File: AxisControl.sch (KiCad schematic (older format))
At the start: 2 parts, among them J14 Max, J15 Min

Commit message: Update annotations.
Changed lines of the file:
@@
 EESchema Schematic File Version 4
 LIBS:PrntrBoardV1-cache
-EELAYER 26 0
+EELAYER 29 0
 EELAYER END
 $Descr A4 11693 8268
@@
 AR Path="/5AC337B6/5ACCA309/5AE0BB35" Ref="J16"  Part="1"
 AR Path="/5AC337B6/5ACE1C6D/5AE0BB35" Ref="J18"  Part="1"
-F 0 "J16" H 6500 3567 50  0000 C CNN
+F 0 "J18" H 6500 3567 50  0000 C CNN
 F 1 "Max" H 6500 3476 50  0000 C CNN
 F 2 "Connector_PinHeader_2.54mm:PinHeader_1x02_P2.54mm_Vertical" H 6450 3350 50  0001 C CNN
@@
 AR Path="/5AC337B6/5ACCA309/5AE0BBC2" Ref="J17"  Part="1"
 AR Path="/5AC337B6/5ACE1C6D/5AE0BBC2" Ref="J19"  Part="1"
-F 0 "J17" H 6500 4217 50  0000 C CNN
+F 0 "J19" H 6500 4217 50  0000 C CNN
 F 1 "Min" H 6500 4126 50  0000 C CNN
 F 2 "Connector_PinHeader_2.54mm:PinHeader_1x02_P2.54mm_Vertical" H 6450 4000 50  0001 C CNN

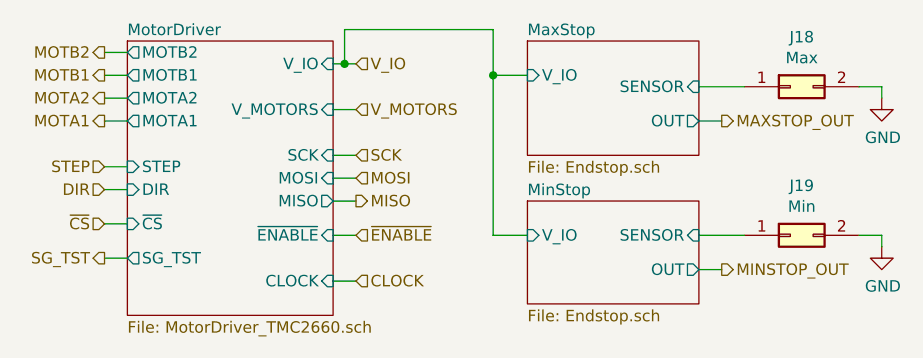
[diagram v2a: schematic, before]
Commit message: Update schematics to match rev3 of tmc2130 branch.
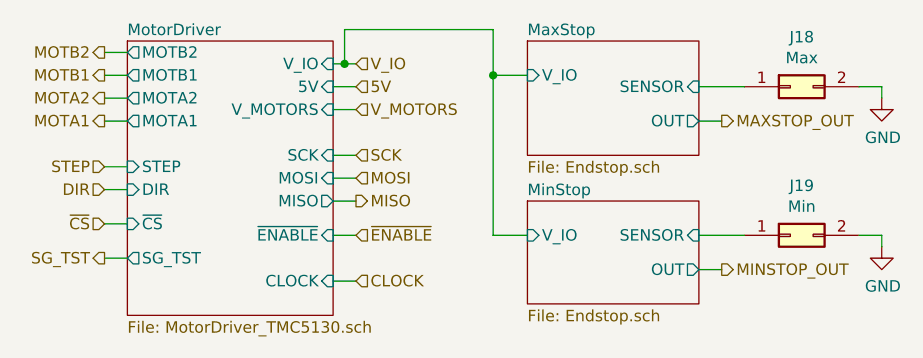
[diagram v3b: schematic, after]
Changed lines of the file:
@@
 $Descr A4 11693 8268
 encoding utf-8
-Sheet 12 35
+Sheet 8 35
 Title ""
 Date ""
@@
 U 5ACC0B66
 F0 "MotorDriver" 50
-F1 "MotorDriver_TMC2660.sch" 50
+F1 "MotorDriver_TMC5130.sch" 50
 F2 "V_IO" I R 4450 3250 50
 F3 "V_MOTORS" I R 4450 3450 50
@@
 F10 "~ENABLE" I R 4450 4000 50
 F11 "SG_TST" O L 3550 4100 50
-F12 "CLOCK" I R 4450 4200 50
-F13 "MOTB1" O L 3550 3300 50
-F14 "MOTA1" O L 3550 3500 50
-F15 "MOTA2" O L 3550 3400 50
-F16 "MOTB2" O L 3550 3200 50
+F12 "5V" I R 4450 3350 50
+F13 "CLOCK" I R 4450 4200 50
+F14 "MOTB1" O L 3550 3300 50
+F15 "MOTA1" O L 3550 3500 50
+F16 "MOTA2" O L 3550 3400 50
+F17 "MOTB2" O L 3550 3200 50
 $EndSheet
 Text HLabel 3450 3500 0    50   Output ~ 0
@@
 Wire Wire Line
 	6250 3350 6050 3350
+Text HLabel 4550 3350 2    50   Input ~ 0
+5V
+Wire Wire Line
+	4550 3350 4450 3350
 Text HLabel 4550 4200 2    50   Input ~ 0
 CLOCK

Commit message: Reset schematics for tmc2660. Clean the board layout.
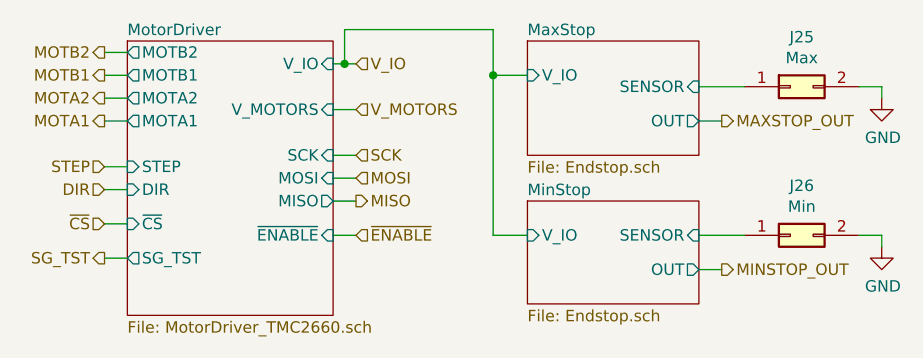
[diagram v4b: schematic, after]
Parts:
- renumbered J14 to J21, J15 to J22
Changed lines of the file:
@@
 U 5ACC0B66
 F0 "MotorDriver" 50
-F1 "MotorDriver_TMC5130.sch" 50
+F1 "MotorDriver_TMC2660.sch" 50
 F2 "V_IO" I R 4450 3250 50
 F3 "V_MOTORS" I R 4450 3450 50
@@
 F10 "~ENABLE" I R 4450 4000 50
 F11 "SG_TST" O L 3550 4100 50
-F12 "5V" I R 4450 3350 50
-F13 "CLOCK" I R 4450 4200 50
-F14 "MOTB1" O L 3550 3300 50
-F15 "MOTA1" O L 3550 3500 50
-F16 "MOTA2" O L 3550 3400 50
-F17 "MOTB2" O L 3550 3200 50
+F12 "MOTB1" O L 3550 3300 50
+F13 "MOTA1" O L 3550 3500 50
+F14 "MOTA2" O L 3550 3400 50
+F15 "MOTB2" O L 3550 3200 50
 $EndSheet
 Text HLabel 3450 3500 0    50   Output ~ 0
@@
 	6050 3500 6150 3500
 $Comp
-L Connector_Generic:Conn_02x01 J14
+L Connector_Generic:Conn_02x01 J21
 U 1 1 5AE0BB35
 P 6450 3350
-AR Path="/5AC337B6/5ACC0AA2/5AE0BB35" Ref="J14"  Part="1"
-AR Path="/5AC337B6/5ACCA309/5AE0BB35" Ref="J16"  Part="1"
-AR Path="/5AC337B6/5ACE1C6D/5AE0BB35" Ref="J18"  Part="1"
-F 0 "J18" H 6500 3567 50  0000 C CNN
+AR Path="/5AC337B6/5ACC0AA2/5AE0BB35" Ref="J21"  Part="1"
+AR Path="/5AC337B6/5ACCA309/5AE0BB35" Ref="J23"  Part="1"
+AR Path="/5AC337B6/5ACE1C6D/5AE0BB35" Ref="J25"  Part="1"
+F 0 "J25" H 6500 3567 50  0000 C CNN
 F 1 "Max" H 6500 3476 50  0000 C CNN
 F 2 "Connector_PinHeader_2.54mm:PinHeader_1x02_P2.54mm_Vertical" H 6450 3350 50  0001 C CNN
@@
 $EndComp
 $Comp
-L Connector_Generic:Conn_02x01 J15
+L Connector_Generic:Conn_02x01 J22
 U 1 1 5AE0BBC2
 P 6450 4000
-AR Path="/5AC337B6/5ACC0AA2/5AE0BBC2" Ref="J15"  Part="1"
-AR Path="/5AC337B6/5ACCA309/5AE0BBC2" Ref="J17"  Part="1"
-AR Path="/5AC337B6/5ACE1C6D/5AE0BBC2" Ref="J19"  Part="1"
-F 0 "J19" H 6500 4217 50  0000 C CNN
+AR Path="/5AC337B6/5ACC0AA2/5AE0BBC2" Ref="J22"  Part="1"
+AR Path="/5AC337B6/5ACCA309/5AE0BBC2" Ref="J24"  Part="1"
+AR Path="/5AC337B6/5ACE1C6D/5AE0BBC2" Ref="J26"  Part="1"
+F 0 "J26" H 6500 4217 50  0000 C CNN
 F 1 "Min" H 6500 4126 50  0000 C CNN
 F 2 "Connector_PinHeader_2.54mm:PinHeader_1x02_P2.54mm_Vertical" H 6450 4000 50  0001 C CNN
@@
 $EndComp
 $Comp
-L power:GND #PWR023
+L power:GND #PWR034
 U 1 1 5AE0BC50
 P 6850 3400
-AR Path="/5AC337B6/5ACC0AA2/5AE0BC50" Ref="#PWR023"  Part="1"
-AR Path="/5AC337B6/5ACCA309/5AE0BC50" Ref="#PWR034"  Part="1"
-AR Path="/5AC337B6/5ACE1C6D/5AE0BC50" Ref="#PWR045"  Part="1"
-F 0 "#PWR045" H 6850 3150 50  0001 C CNN
+AR Path="/5AC337B6/5ACC0AA2/5AE0BC50" Ref="#PWR034"  Part="1"
+AR Path="/5AC337B6/5ACCA309/5AE0BC50" Ref="#PWR045"  Part="1"
+AR Path="/5AC337B6/5ACE1C6D/5AE0BC50" Ref="#PWR056"  Part="1"
+F 0 "#PWR056" H 6850 3150 50  0001 C CNN
 F 1 "GND" H 6855 3227 50  0000 C CNN
 F 2 "" H 6850 3400 50  0001 C CNN
@@
 $EndComp
 $Comp
-L power:GND #PWR024
+L power:GND #PWR035
 U 1 1 5AE0BC78
 P 6850 4050
-AR Path="/5AC337B6/5ACC0AA2/5AE0BC78" Ref="#PWR024"  Part="1"
-AR Path="/5AC337B6/5ACCA309/5AE0BC78" Ref="#PWR035"  Part="1"
-AR Path="/5AC337B6/5ACE1C6D/5AE0BC78" Ref="#PWR046"  Part="1"
-F 0 "#PWR046" H 6850 3800 50  0001 C CNN
+AR Path="/5AC337B6/5ACC0AA2/5AE0BC78" Ref="#PWR035"  Part="1"
+AR Path="/5AC337B6/5ACCA309/5AE0BC78" Ref="#PWR046"  Part="1"
+AR Path="/5AC337B6/5ACE1C6D/5AE0BC78" Ref="#PWR057"  Part="1"
+F 0 "#PWR057" H 6850 3800 50  0001 C CNN
 F 1 "GND" H 6855 3877 50  0000 C CNN
 F 2 "" H 6850 4050 50  0001 C CNN
@@
 Wire Wire Line
 	6250 3350 6050 3350
-Text HLabel 4550 3350 2    50   Input ~ 0
-5V
-Wire Wire Line
-	4550 3350 4450 3350
-Text HLabel 4550 4200 2    50   Input ~ 0
-CLOCK
-Wire Wire Line
-	4550 4200 4450 4200
 $EndSCHEMATC

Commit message: Updated component values, updated component footprint.
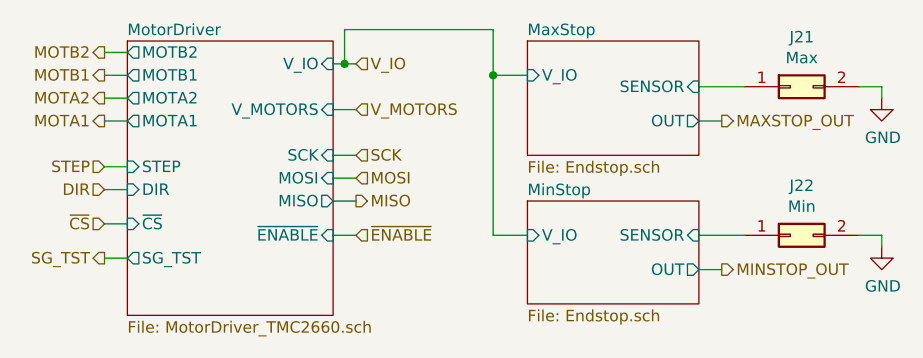
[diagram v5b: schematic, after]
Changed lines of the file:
@@
 AR Path="/5AC337B6/5ACCA309/5AE0BB35" Ref="J23"  Part="1"
 AR Path="/5AC337B6/5ACE1C6D/5AE0BB35" Ref="J25"  Part="1"
-F 0 "J25" H 6500 3567 50  0000 C CNN
+F 0 "J21" H 6500 3567 50  0000 C CNN
 F 1 "Max" H 6500 3476 50  0000 C CNN
 F 2 "Connector_PinHeader_2.54mm:PinHeader_1x02_P2.54mm_Vertical" H 6450 3350 50  0001 C CNN
@@
 AR Path="/5AC337B6/5ACCA309/5AE0BBC2" Ref="J24"  Part="1"
 AR Path="/5AC337B6/5ACE1C6D/5AE0BBC2" Ref="J26"  Part="1"
-F 0 "J26" H 6500 4217 50  0000 C CNN
+F 0 "J22" H 6500 4217 50  0000 C CNN
 F 1 "Min" H 6500 4126 50  0000 C CNN
 F 2 "Connector_PinHeader_2.54mm:PinHeader_1x02_P2.54mm_Vertical" H 6450 4000 50  0001 C CNN

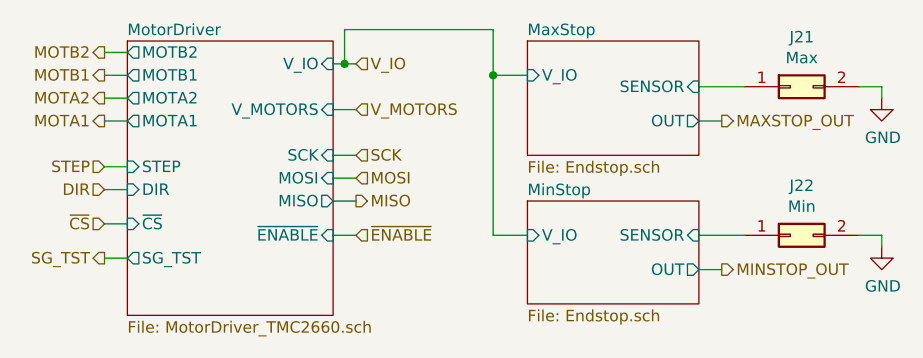
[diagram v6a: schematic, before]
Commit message: Added reverse polarity input protection diodes. Re-routed input power.
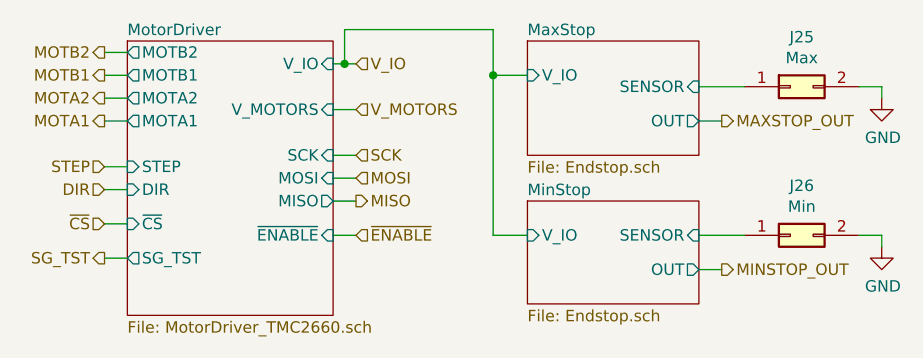
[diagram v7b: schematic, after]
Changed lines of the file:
@@
 AR Path="/5AC337B6/5ACCA309/5AE0BB35" Ref="J23"  Part="1"
 AR Path="/5AC337B6/5ACE1C6D/5AE0BB35" Ref="J25"  Part="1"
-F 0 "J21" H 6500 3567 50  0000 C CNN
+F 0 "J25" H 6500 3567 50  0000 C CNN
 F 1 "Max" H 6500 3476 50  0000 C CNN
 F 2 "Connector_PinHeader_2.54mm:PinHeader_1x02_P2.54mm_Vertical" H 6450 3350 50  0001 C CNN
@@
 AR Path="/5AC337B6/5ACCA309/5AE0BBC2" Ref="J24"  Part="1"
 AR Path="/5AC337B6/5ACE1C6D/5AE0BBC2" Ref="J26"  Part="1"
-F 0 "J22" H 6500 4217 50  0000 C CNN
+F 0 "J26" H 6500 4217 50  0000 C CNN
 F 1 "Min" H 6500 4126 50  0000 C CNN
 F 2 "Connector_PinHeader_2.54mm:PinHeader_1x02_P2.54mm_Vertical" H 6450 4000 50  0001 C CNN

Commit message: Added clock source for the TMC2660 drivers.
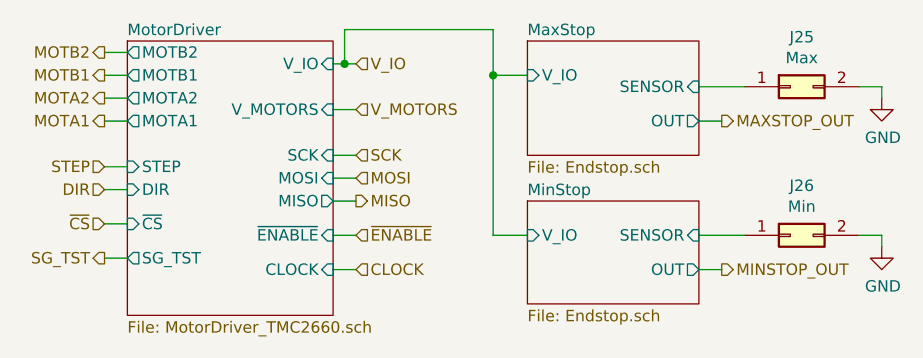
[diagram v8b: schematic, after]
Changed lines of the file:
@@
 $Descr A4 11693 8268
 encoding utf-8
-Sheet 8 35
+Sheet 12 35
 Title ""
 Date ""
@@
 F14 "MOTA2" O L 3550 3400 50
 F15 "MOTB2" O L 3550 3200 50
+F16 "CLOCK" I R 4450 4150 50
 $EndSheet
 Text HLabel 3450 3500 0    50   Output ~ 0
@@
 Wire Wire Line
 	6250 3350 6050 3350
+Text HLabel 4550 4150 2    50   Input ~ 0
+CLOCK
+Wire Wire Line
+	4550 4150 4450 4150
 $EndSCHEMATC
